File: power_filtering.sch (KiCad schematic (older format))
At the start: 108 parts

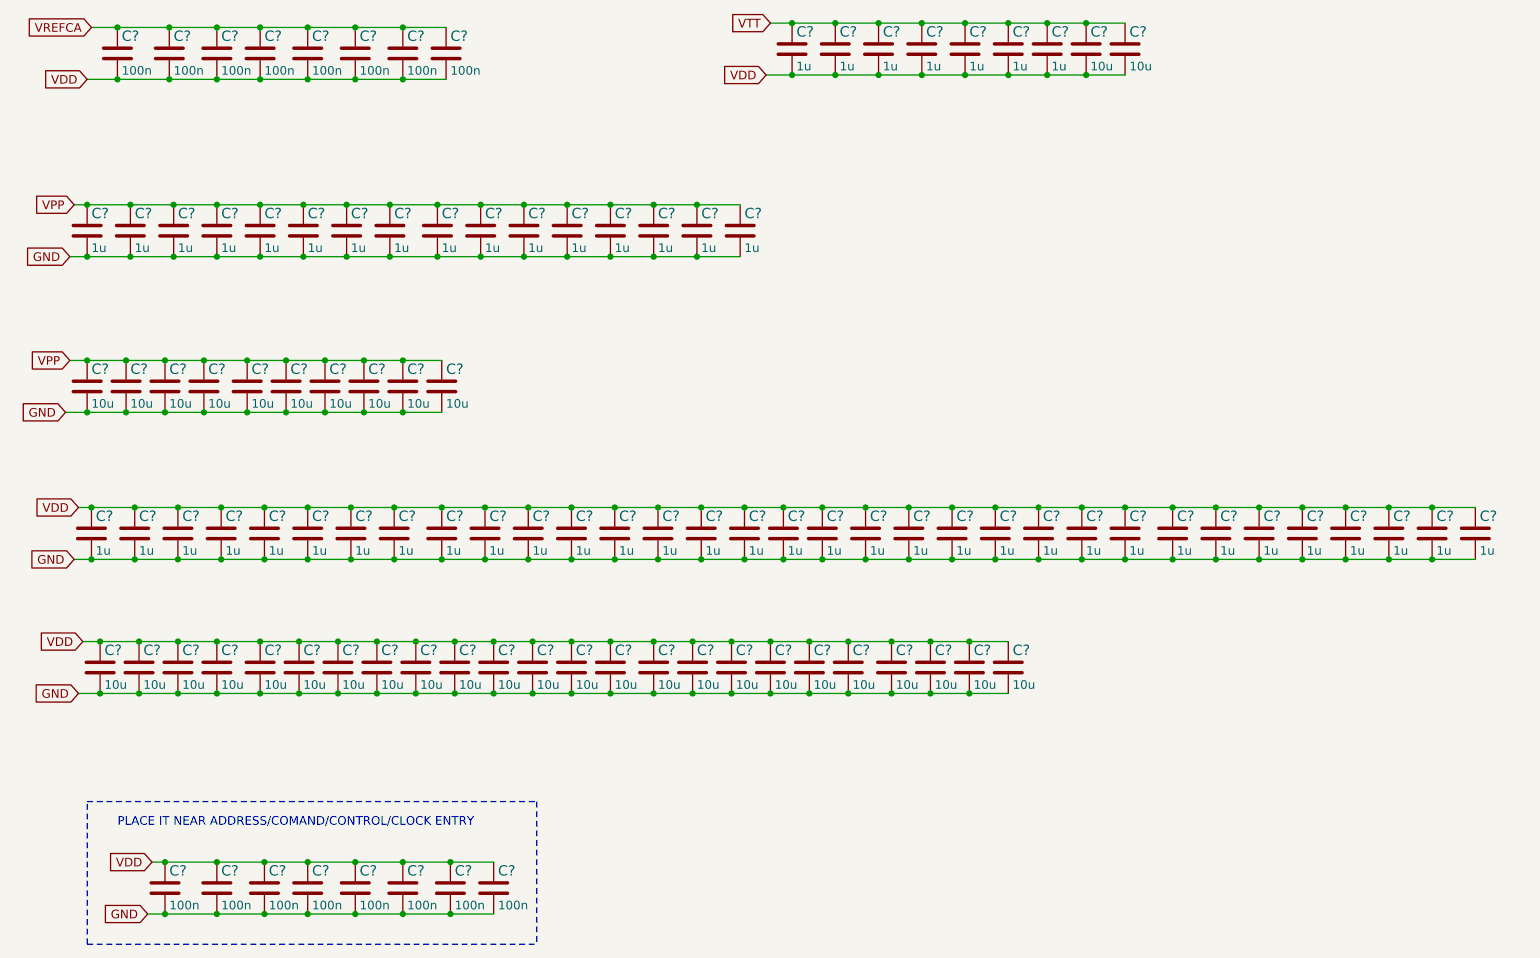
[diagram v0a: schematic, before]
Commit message: Remove data resistors sheet and add notes
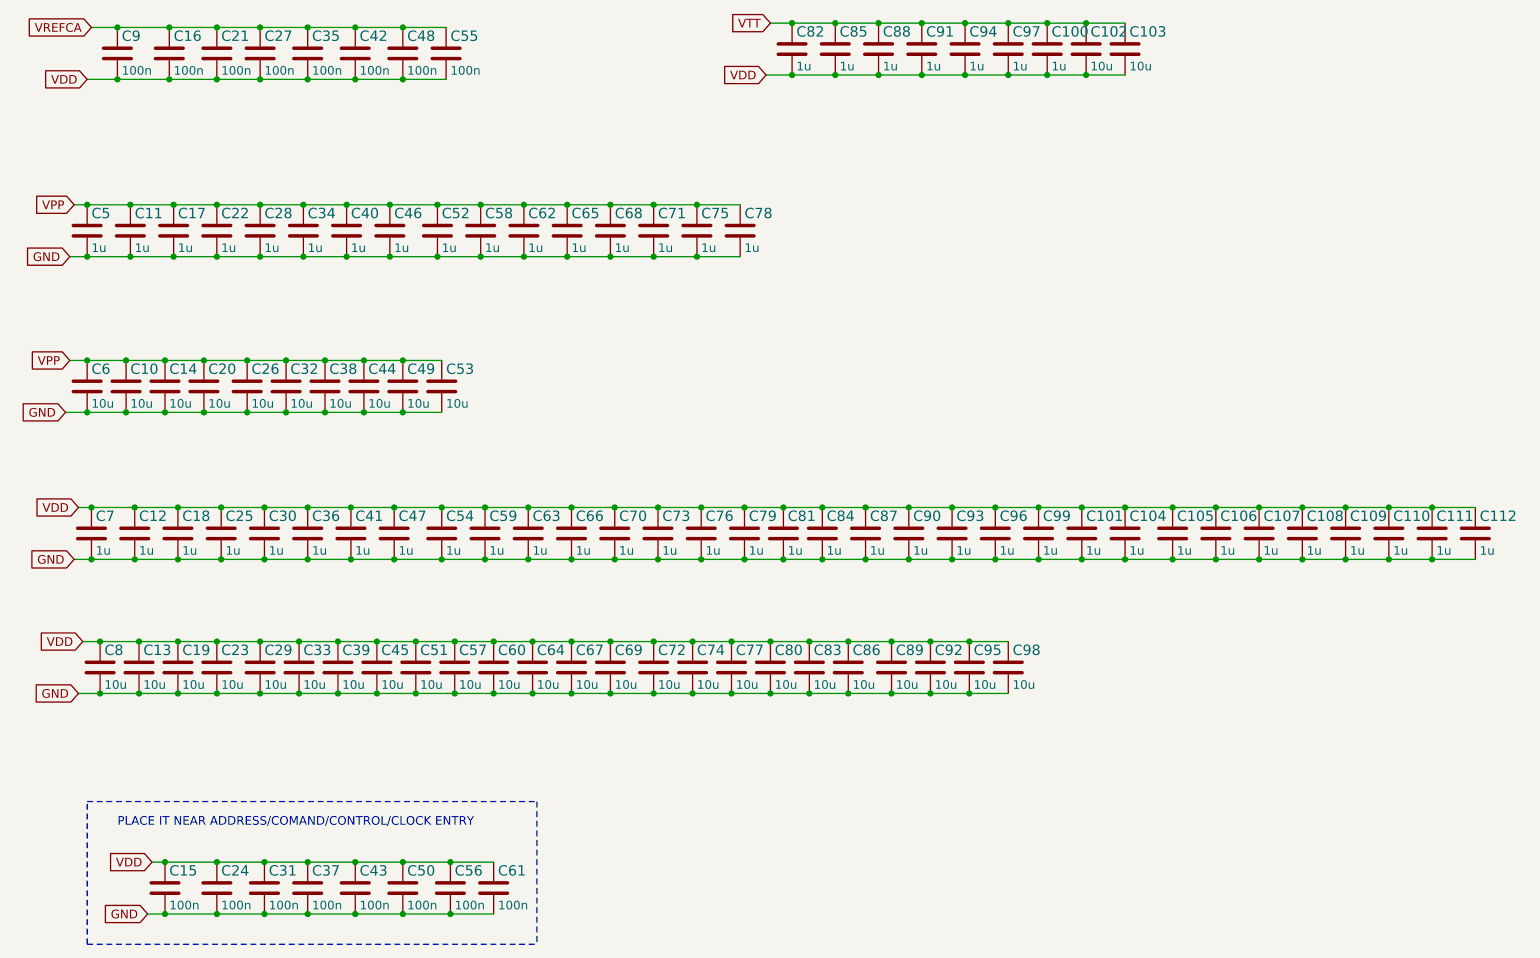
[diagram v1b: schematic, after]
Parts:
- gave numbers to parts that had none: 108
